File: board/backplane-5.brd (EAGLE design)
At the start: 100 x 100 mm, 142 parts, among them CN1 RJ45JACK90, U1 AMS1117-5.0, U10 RT9193, U11 KSZ9897, U12 KSZ8081MLX, U2 AMS1117-5.0, U3 AMS1117-5.0, U4 AMS1117-5.0, U5 AMS1117-5.0, U6 AMS1117-2.5, U7 AMS1117-1.2, U8 RT9193, U9 AMS1117-5.0, X1 25MHz, X2 25MHz

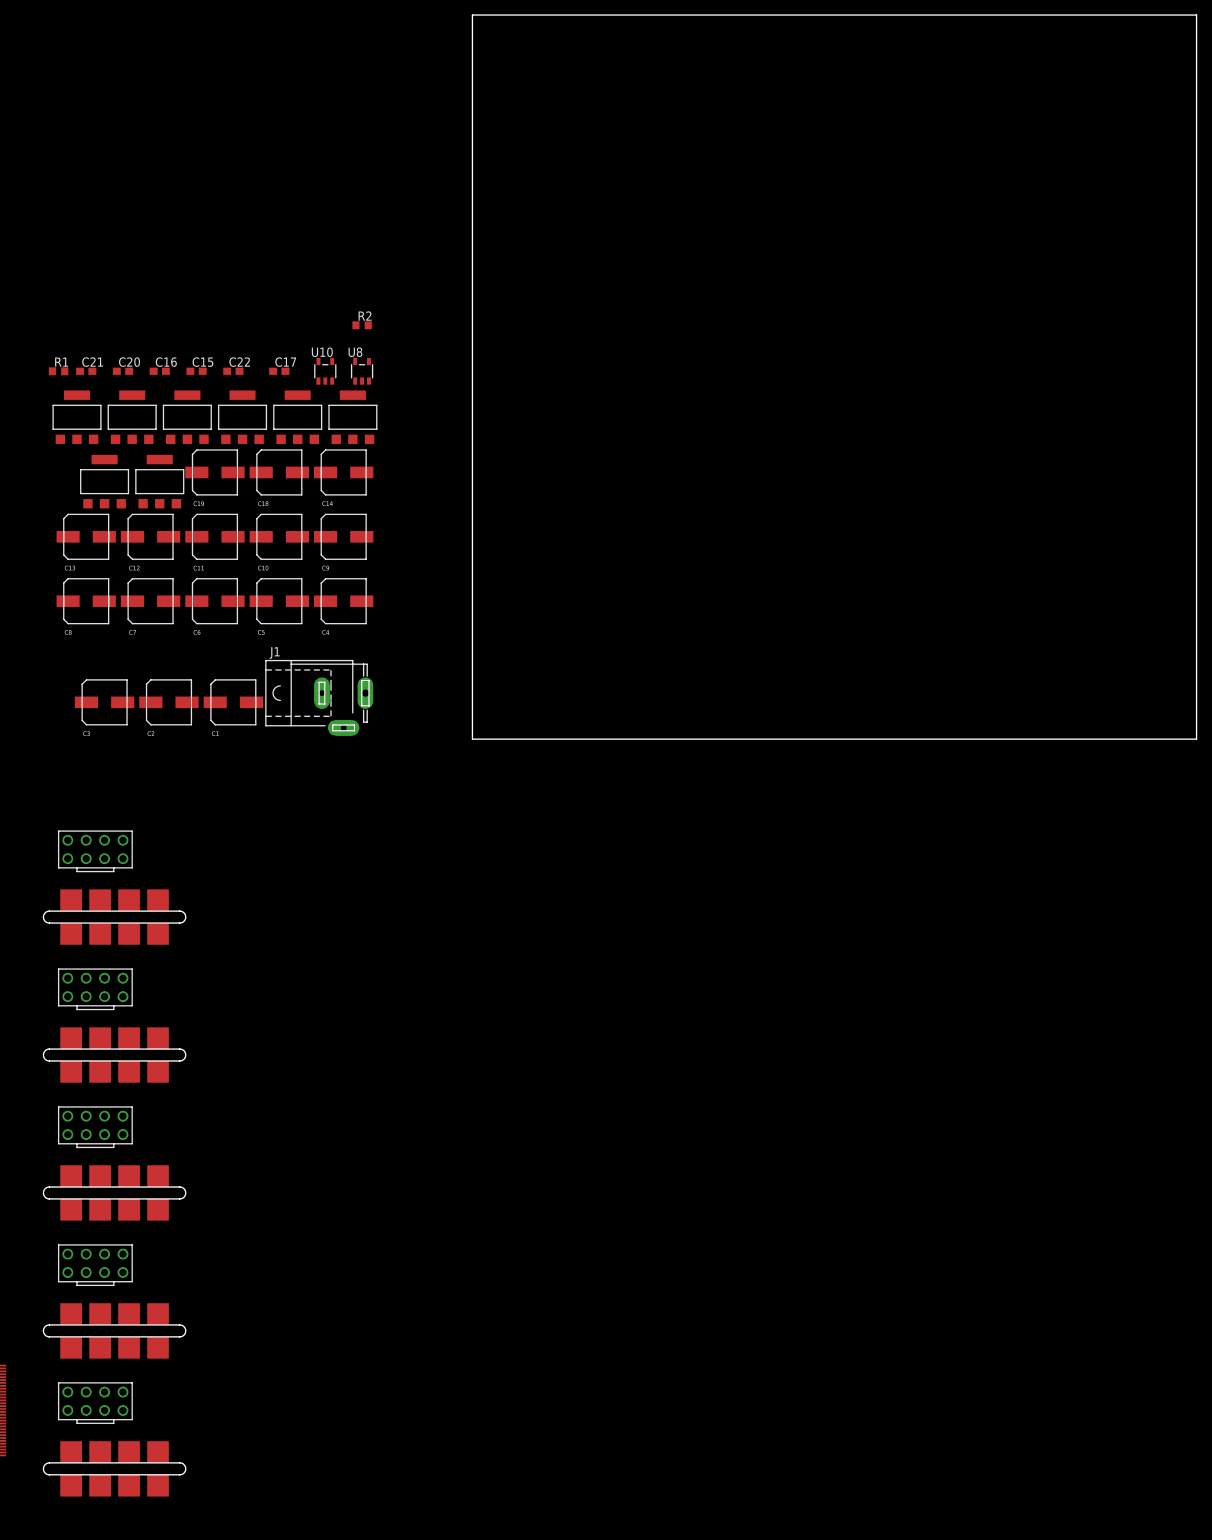
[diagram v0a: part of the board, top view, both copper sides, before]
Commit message: Tweaked some packages and placed RPi conn
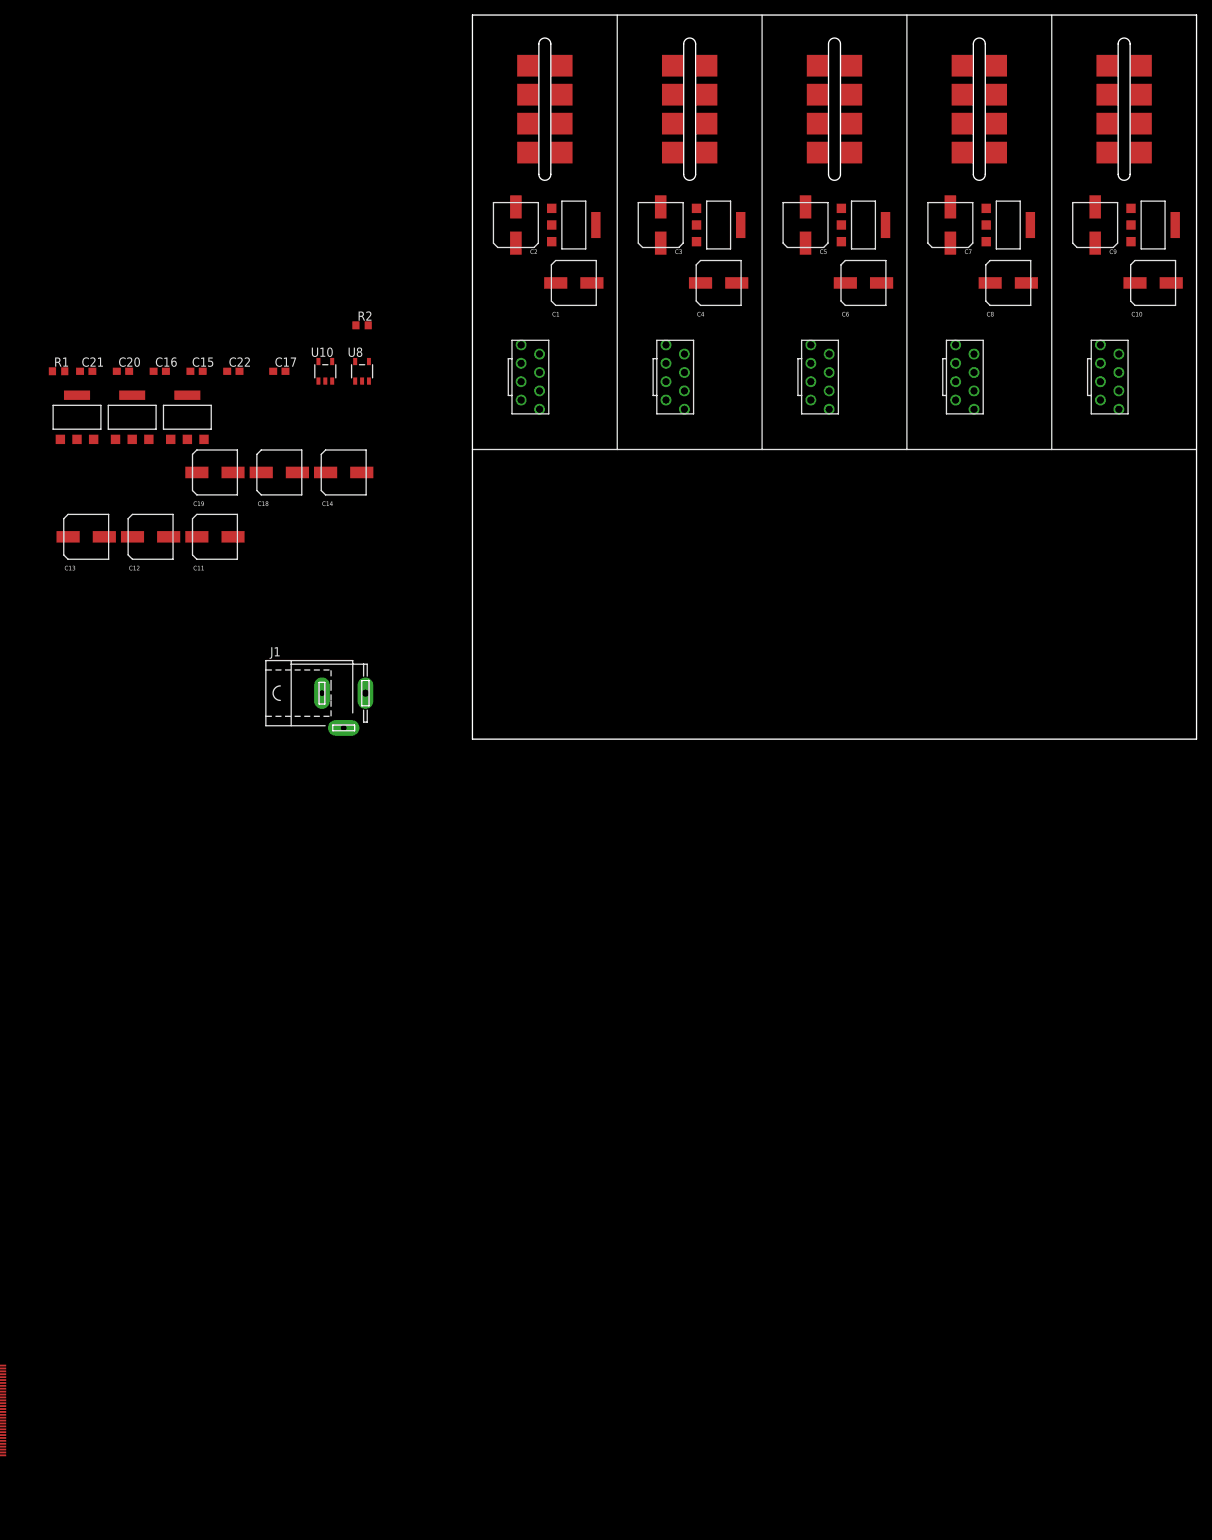
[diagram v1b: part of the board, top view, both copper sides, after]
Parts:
- moved U$5 240.0 mm to (90.0, 87.0), turned to 90 degrees
- moved U$4 212.7 mm to (70.0, 87.0), turned to 90 degrees
- moved RJ5 199.1 mm to (88.0, 50.0), turned to 270 degrees
- moved U$3 185.5 mm to (50.0, 87.0), turned to 90 degrees
- moved RJ4 171.5 mm to (68.0, 50.0), turned to 270 degrees
- moved U$2 158.4 mm to (30.0, 87.0), turned to 90 degrees
- moved RJ3 143.9 mm to (48.0, 50.0), turned to 270 degrees
- moved C8 134.7 mm to (74.0, 63.0)
- moved U$1 131.6 mm to (10.0, 87.0), turned to 90 degrees
- moved U5 128.5 mm to (94.0, 71.0), turned to 270 degrees
- moved C10 125.7 mm to (94.0, 63.0)
- moved C7 122.1 mm to (66.0, 71.0), turned to 90 degrees
- moved RJ2 116.3 mm to (28.0, 50.0), turned to 270 degrees
- moved C9 112.4 mm to (86.0, 71.0), turned to 90 degrees
- moved U4 101.7 mm to (74.0, 71.0), turned to 270 degrees
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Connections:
- net PE: now also CN1.S@1, CN1.S@2

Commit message: Fixed led connection
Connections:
- net PHY5LED0: now also CN1.10; no longer R25.2
- net PHY5LED1: now also CN1.12; no longer R26.2
- net PHY6LED0: now also R25.2; no longer CN1.10
- net PHY6LED1: now also R26.2; no longer CN1.12
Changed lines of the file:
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@@
 </signal>
 <signal name="PHY6LED0">
-<contactref element="CN1" pad="10"/>
 <contactref element="U12" pad="42"/>
-<wire x1="-99.5" y1="-255.02" x2="-90.805" y2="-330.835" width="0" layer="19" extent="1-1"/>
+<contactref element="R25" pad="2"/>
+<wire x1="-141.39" y1="-466.09" x2="-99.5" y2="-255.02" width="0" layer="19" extent="1-1"/>
 </signal>
 <signal name="PHY6LED1">
-<contactref element="CN1" pad="12"/>
 <contactref element="U12" pad="43"/>
-<wire x1="-99.5" y1="-255.52" x2="-79.375" y2="-330.835" width="0" layer="19" extent="1-1"/>
+<contactref element="R26" pad="2"/>
+<wire x1="-99.5" y1="-255.52" x2="-145.2" y2="-473.71" width="0" layer="19" extent="1-1"/>
 </signal>
 <signal name="N$13">
@@
 <signal name="PHY5LED0">
 <contactref element="U11" pad="P$102"/>
-<contactref element="R25" pad="2"/>
-<wire x1="-141.39" y1="-466.09" x2="-68.19" y2="-85.11" width="0" layer="19" extent="1-1"/>
+<contactref element="CN1" pad="10"/>
+<wire x1="-68.19" y1="-85.11" x2="-90.805" y2="-330.835" width="0" layer="19" extent="1-1"/>
 </signal>
 <signal name="PHY5LED1">
 <contactref element="U11" pad="P$103"/>
-<contactref element="R26" pad="2"/>
-<wire x1="-145.2" y1="-473.71" x2="-68.59" y2="-85.11" width="0" layer="19" extent="1-1"/>
+<contactref element="CN1" pad="12"/>
+<wire x1="-68.59" y1="-85.11" x2="-79.375" y2="-330.835" width="0" layer="19" extent="1-1"/>
 </signal>
 <signal name="MDC">

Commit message: Laid out some psus
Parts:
- moved CN1 410.1 mm to (93.9, 28.0), turned to 90 degrees
- moved U12 310.6 mm to (29.3, 29.3), turned to 270 degrees
- moved C25 235.7 mm to (79.2, 30.5)
- moved C26 229.8 mm to (79.2, 27.2)
- moved X1 223.0 mm to (75.6, 28.9), turned to 90 degrees
- moved U11 179.2 mm to (58.9, 29.3), turned to 270 degrees
- moved U6 116.7 mm to (70.5, 5.00), turned to 180 degrees
- moved C11 115.2 mm to (77.5, 6.00), turned to 270 degrees
- moved C13 112.0 mm to (56.5, 6.00), turned to 270 degrees
- moved C12 110.2 mm to (63.5, 6.00), turned to 270 degrees
- moved J1 107.0 mm to (89.0, 12.6), turned to 180 degrees
- moved U7 104.4 mm to (49.5, 4.50), turned to 180 degrees
- moved U9 82.7 mm to (18.9, 6.45)
- moved C1 80.0 mm to (94.0, 63.0)
- moved C10 80.0 mm to (14.0, 63.0)
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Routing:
- net 5V-5: track 0.00 -> 25.5 mm
- net 5V-1: track 0.00 -> 25.5 mm
- net 5V-4: track 0.00 -> 25.4 mm
- net 5V-2: track 0.00 -> 25.4 mm
- net 5V-3: track 0.00 -> 25.3 mm
- net 5V: track 0.00 -> 7.78 mm
- net 12V: track 0.00 -> 5.93 mm
- net N$3: track 0.00 -> 1.53 mm
- net 3V3-PHY: track 0.00 -> 1.53 mm
- net 3V3-LED: track 0.00 -> 1.53 mm
- net N$1: track 0.00 -> 1.53 mm
- net N$4: track 0.00 -> 1.51 mm
- net N$2: track 0.00 -> 1.51 mm

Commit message: Placed some decoupling caps on the board
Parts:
- moved C56 312.3 mm to (63.8, 24.4), flipped to the bottom
- moved C52 312.0 mm to (63.8, 34.1), flipped to the bottom, turned to 270 degrees
- moved C54 303.3 mm to (54.1, 24.4), flipped to the bottom, turned to 180 degrees
- moved C50 302.2 mm to (63.8, 28.0), flipped to the bottom
- moved C51 301.8 mm to (63.8, 31.7), flipped to the bottom
- moved C46 297.5 mm to (61.4, 34.1), flipped to the bottom, turned to 270 degrees
- moved C48 296.3 mm to (54.1, 31.7), flipped to the bottom, turned to 180 degrees
- moved C55 295.5 mm to (57.3, 17.9), turned to 270 degrees
- moved C47 291.5 mm to (56.5, 34.1), flipped to the bottom, turned to 270 degrees
- moved C49 289.5 mm to (54.1, 28.0), flipped to the bottom, turned to 180 degrees
- moved C44 285.0 mm to (54.1, 34.1), flipped to the bottom, turned to 270 degrees
- moved C43 284.1 mm to (69.9, 33.3)
- moved C42 282.5 mm to (63.8, 30.5), flipped to the bottom
- moved C38 273.7 mm to (57.7, 34.1), flipped to the bottom, turned to 270 degrees
- moved C41 273.1 mm to (63.8, 29.3), flipped to the bottom
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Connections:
- removed net PE: C23.2, C24.2, C27.2, C28.2, C29.2, C30.2, C31.2, C32.2, C33.2, C34.2, C35.2, C36.2, C37.2, C38.2, C39.2, C40.2, C41.2, C42.2, C43.2, C44.2, C45.2, C46.2, C47.2, C48.2, C49.2, C50.2, C51.2, C52.2, C53.2, C54.2, C55.2, C56.2, C57.2, CN1.S@1, CN1.S@2
- net 2V5: now also C54.1, C55.1, C56.1, C57.1
- net 2V5-A: no longer C54.1, C55.1, C56.1, C57.1
- net GND: now also C23.2, C24.2, C27.2, C28.2, C29.2, C30.2, C31.2, C32.2, C33.2, C34.2, C35.2, C36.2, C37.2, C38.2, C39.2, C40.2, C41.2, C42.2, C43.2, C44.2, C45.2, C46.2, C47.2, C48.2, C49.2, C50.2, C51.2, C52.2, C53.2, C54.2, C55.2, C56.2, C57.2, CN1.S@1, CN1.S@2

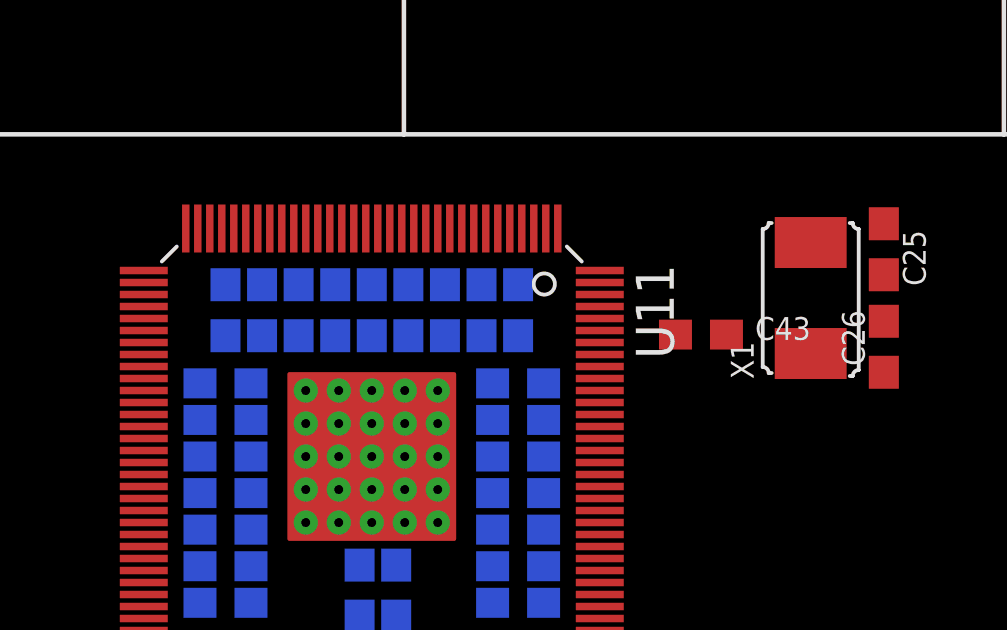
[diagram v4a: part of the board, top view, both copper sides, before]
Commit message: Tweaked a bit the caps
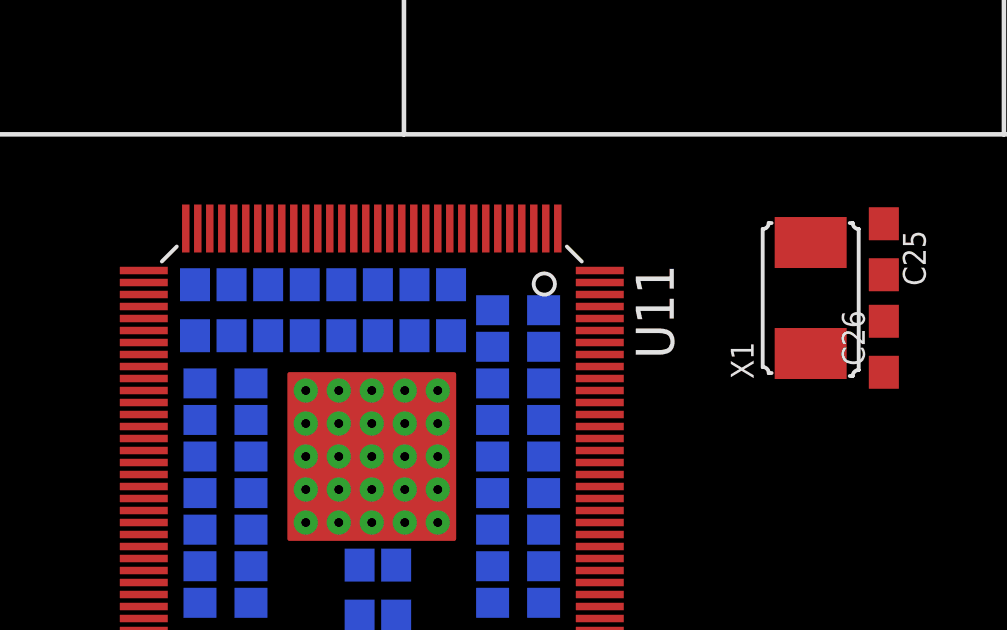
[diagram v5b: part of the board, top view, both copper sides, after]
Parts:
- moved C43 6.11 mm to (63.8, 32.9), flipped to the bottom
- moved C28 1.02 mm to (54.3, 34.1)
- moved C47 1.02 mm to (55.5, 34.1)
- moved C27 1.02 mm to (59.1, 34.1)
- moved C36 1.02 mm to (61.6, 34.1)
- moved C37 1.02 mm to (57.9, 34.1)
- moved C38 1.02 mm to (56.7, 34.1)
- moved C44 1.02 mm to (53.0, 34.1)
- moved C46 1.02 mm to (60.4, 34.1)
- turned C52 to 0 degrees

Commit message: Routed switch resistors
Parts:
- C59, C61: value 1uF -> 100n
- moved R32 583.5 mm to (68.7, 23.2), turned to 90 degrees
- moved R4 319.5 mm to (70.3, 23.2), turned to 90 degrees
- moved C58 319.4 mm to (66.6, 20.7), turned to 270 degrees
- moved R3 238.2 mm to (69.5, 36.6), turned to 270 degrees
- moved C25 4.88 mm to (71.1, 36.2), turned to 90 degrees
- moved C26 4.88 mm to (71.1, 32.9), turned to 270 degrees
- moved U12 3.45 mm to (31.7, 26.8)
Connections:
- net 2V5: now also C61.1, C62.1
- net 3V3-PHY: no longer C61.1, C62.1
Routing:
- net N$5: track 0.00 -> 7.75 mm
- net N$6: track 0.00 -> 7.68 mm
- net N$8: track 0.00 -> 5.70 mm
- net MDIO: track 0.00 -> 5.56 mm
- net 2V5: track 0.00 -> 3.84 mm
- net N$7: track 0.00 -> 3.24 mm

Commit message: Connected decoupling caps on the switch
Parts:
- moved R16 460.4 mm to (31.7, 19.1), turned to 270 degrees
- moved R5 357.0 mm to (30.1, 19.1), turned to 90 degrees
- moved C64 346.6 mm to (39.8, 27.2)
- moved C65 346.4 mm to (22.8, 28.9), turned to 180 degrees
- moved C67 346.3 mm to (24.4, 15.4), turned to 270 degrees
- moved C66 342.8 mm to (27.6, 15.4), turned to 270 degrees
- moved X2 338.5 mm to (26.0, 19.1), turned to 180 degrees
- moved C62 333.2 mm to (39.8, 22.8), turned to 270 degrees
- moved C61 327.9 mm to (38.2, 22.8), turned to 270 degrees
- moved C60 319.7 mm to (22.8, 25.6), turned to 180 degrees
- moved C59 316.5 mm to (22.8, 27.2), turned to 180 degrees
- moved C23 186.0 mm to (45.7, 31.4)
- moved C25 5.30 mm to (75.6, 39.0), turned to 0 degrees
- moved C26 5.09 mm to (75.6, 35.4), turned to 0 degrees
- moved X1 3.00 mm to (72.1, 37.2)
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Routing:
- net 1V2-A: track 0.00 -> 72.9 mm, vias 0 -> 9
- net 1V2: track 0.00 -> 64.3 mm, vias 0 -> 8
- net 2V5-A: track 0.00 -> 54.1 mm, vias 0 -> 7
- net 2V5: track 3.84 -> 22.7 mm, vias 0 -> 2
- net N$10: track 0.00 -> 10.7 mm
- net N$9: track 0.00 -> 10.5 mm
- net PHY2->PI2_P: track 0.00 -> 8.89 mm
- net PHY2->PI2_N: track 0.00 -> 8.88 mm
- net PI2->PHY2_P: track 0.00 -> 6.19 mm
- net PI2->PHY2_N: track 0.00 -> 5.88 mm
- net 3V3-PHY: track 1.53 -> 7.27 mm
- net PI3->PHY3_P: track 0.00 -> 5.46 mm
- net PI4->PHY4_N: track 0.00 -> 5.18 mm
- net PI4->PHY4_P: track 0.00 -> 5.16 mm
- net PI3->PHY3_N: track 0.00 -> 5.14 mm
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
